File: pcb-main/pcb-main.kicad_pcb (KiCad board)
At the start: 2 copper layers, 86 x 86 mm, 37 parts, among them J1 AVR-ISP-6, J2 Conn_02x06_Counter_Clockwise, M1 Stepper_Motor, SW1 SW_MEC_5E, SW2 SW_MEC_5E, U1 ATmega328P-AU, U2 HT1621B-LQFP-A, U3 VIM878, U4 PCF8563T, Y1 16MHz, Y2 32kHz

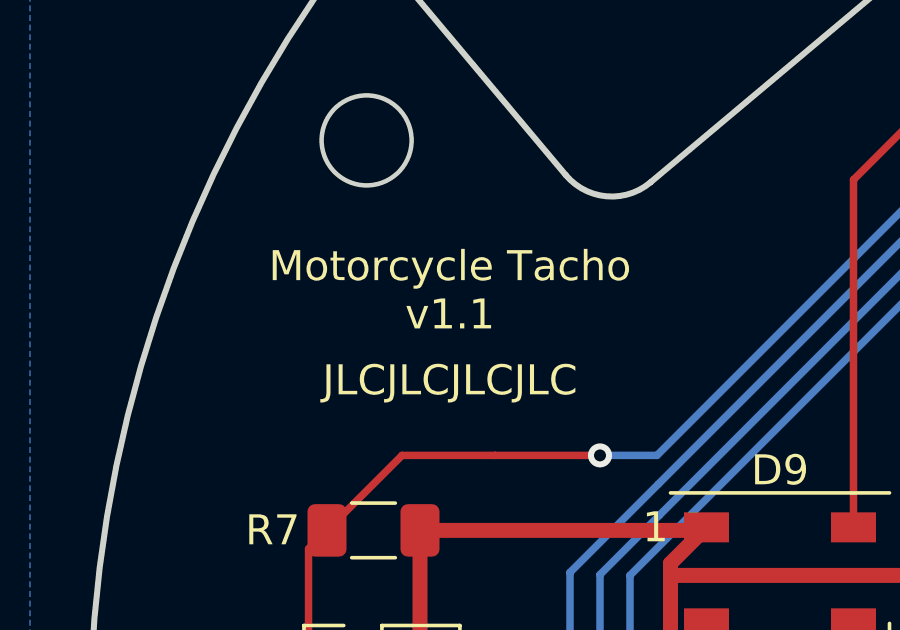
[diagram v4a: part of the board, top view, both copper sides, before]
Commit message: resolves #47: update silkscreen labels
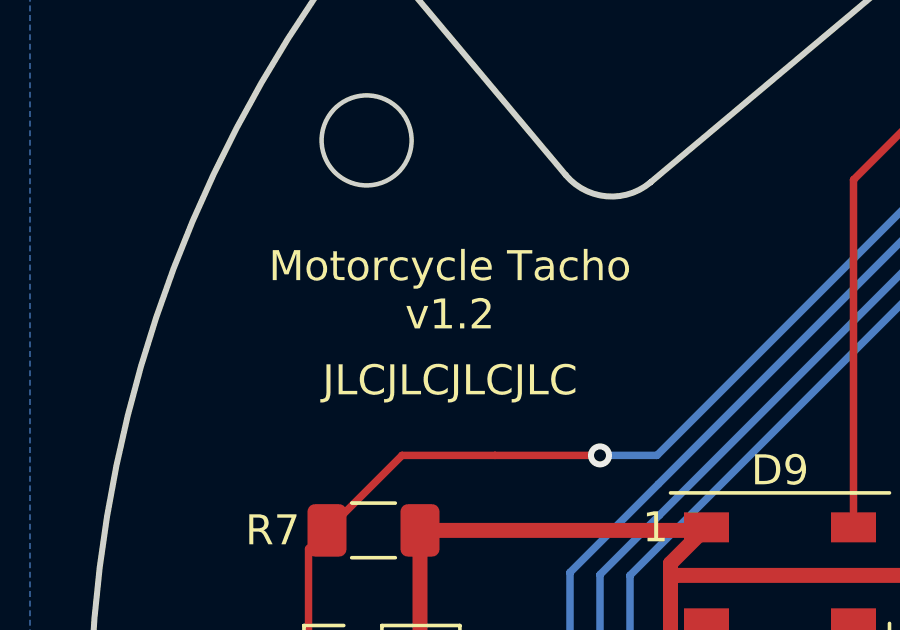
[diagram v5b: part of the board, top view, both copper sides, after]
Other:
- board text added: "Motorcycle Tacho v1.2"
- board text removed: "Motorcycle Tacho v1.1"
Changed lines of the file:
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@@
     (effects (font (size 1 1) (thickness 0.15)) (justify right))
   )
-  (gr_text "Motorcycle Tacho\nv1.1" (at 119 85.5) (layer "F.SilkS")
+  (gr_text "Motorcycle Tacho\nv1.2" (at 119 85.5) (layer "F.SilkS")
     (effects (font (size 1 1) (thickness 0.15)))
   )
